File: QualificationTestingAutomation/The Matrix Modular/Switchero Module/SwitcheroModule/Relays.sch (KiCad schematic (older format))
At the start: 5 parts, among them Q1 2N7002DW, U10 TLP3546, U11 TLP3546

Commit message: Cleaned up the libraries Cleaned up the tracks Adjusted footprints to the manufacturers minimum size.
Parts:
- Q1: symbol TheMatrix-rescue:2N7002DW-dk_Transistors-FETs-MOSFETs-Arrays-SchematicAutomation-rescue -> SwitcheroModule-rescue:2N7002DW-dk_Transistors-FETs-MOSFETs-Arrays-SchematicAutomation-rescue-TheMatrix-rescue
- R5, R6: symbol TheMatrix-rescue:RESISTOR-passive-SchematicAutomation-rescue -> SwitcheroModule-rescue:RESISTOR-passive-SchematicAutomation-rescue-TheMatrix-rescue
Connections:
- wire segments 23 -> 25
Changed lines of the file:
@@
 1_Vin
 $Comp
-L TheMatrix-rescue:RESISTOR-passive-SchematicAutomation-rescue R?
+L SwitcheroModule-rescue:RESISTOR-passive-SchematicAutomation-rescue-TheMatrix-rescue R?
 U 1 1 5CB300C6
 P 9650 4900
@@
 	9850 5200 9450 5200
 $Comp
-L TheMatrix-rescue:RESISTOR-passive-SchematicAutomation-rescue R?
+L SwitcheroModule-rescue:RESISTOR-passive-SchematicAutomation-rescue-TheMatrix-rescue R?
 U 1 1 5CB300E1
 P 8500 5500
@@
 	8250 5500 8250 5600
 $Comp
-L power:GND #PWR?
-U 1 1 5CB300F1
-P 9450 5500
-AR Path="/5C90F514/5CB300F1" Ref="#PWR?"  Part="1"
-AR Path="/5C8DF48C/5CB300F1" Ref="#PWR0115"  Part="1"
-F 0 "#PWR0115" H 9450 5250 50  0001 C CNN
-F 1 "GND" H 9455 5327 50  0000 C CNN
-F 2 "" H 9450 5500 50  0001 C CNN
-F 3 "" H 9450 5500 50  0001 C CNN
-	1    9450 5500
-	-1   0    0    1
-$EndComp
-$Comp
 L power:GND #PWR0116
 U 1 1 5CB33E67
@@
 Wire Wire Line
 	9350 3200 9300 3200
-$Comp
-L power:GND #PWR0118
-U 1 1 5CB3980B
-P 8500 4800
-F 0 "#PWR0118" H 8500 4550 50  0001 C CNN
-F 1 "GND" H 8505 4627 50  0000 C CNN
-F 2 "" H 8500 4800 50  0001 C CNN
-F 3 "" H 8500 4800 50  0001 C CNN
-	1    8500 4800
-	-1   0    0    1
-$EndComp
 Wire Wire Line
 	8500 4900 8500 4800
@@
 	8500 4900 8850 4900
 $Comp
-L TheMatrix-rescue:2N7002DW-dk_Transistors-FETs-MOSFETs-Arrays-SchematicAutomation-rescue Q?
+L SwitcheroModule-rescue:2N7002DW-dk_Transistors-FETs-MOSFETs-Arrays-SchematicAutomation-rescue-TheMatrix-rescue Q?
 U 1 1 5CB300A0
 P 9150 5300
@@
 AR Path="/5C90F514/5CB300A0" Ref="Q?"  Part="1"
 AR Path="/5C8DF48C/5CB300A0" Ref="Q1"  Part="1"
+AR Path="/5CB300A0" Ref="Q1"  Part="1"
 F 0 "Q1" H 9150 5787 60  0000 C CNN
 F 1 "2N7002DW" H 9150 5681 60  0000 C CNN
@@
 Wire Wire Line
 	9550 4900 9450 4900
-Wire Wire Line
-	8850 5500 8700 5500
 Text GLabel 8100 5200 0    50   Input ~ 0
 2_REL
@@
 	8100 5200 8850 5200
 Wire Wire Line
-	8700 5500 8700 5600
-Connection ~ 8700 5500
-Wire Wire Line
-	8700 5500 8600 5500
-Text Label 8700 5600 3    50   ~ 0
+	9600 5500 9600 5600
+Text Label 9600 5600 3    50   ~ 0
 1_RELH
 Text Label 8250 3050 1    50   ~ 0
 1_RELH
-Text Label 9550 4750 1    50   ~ 0
+Text Label 8250 4550 1    50   ~ 0
 2_RELH
 Wire Wire Line
@@
 Text Label 9350 3000 1    50   ~ 0
 2_RELH
+Wire Wire Line
+	8600 5500 8850 5500
+Wire Wire Line
+	9600 5500 9450 5500
+Wire Wire Line
+	8500 4800 8250 4800
+Wire Wire Line
+	8250 4800 8250 4550
 $EndSCHEMATC

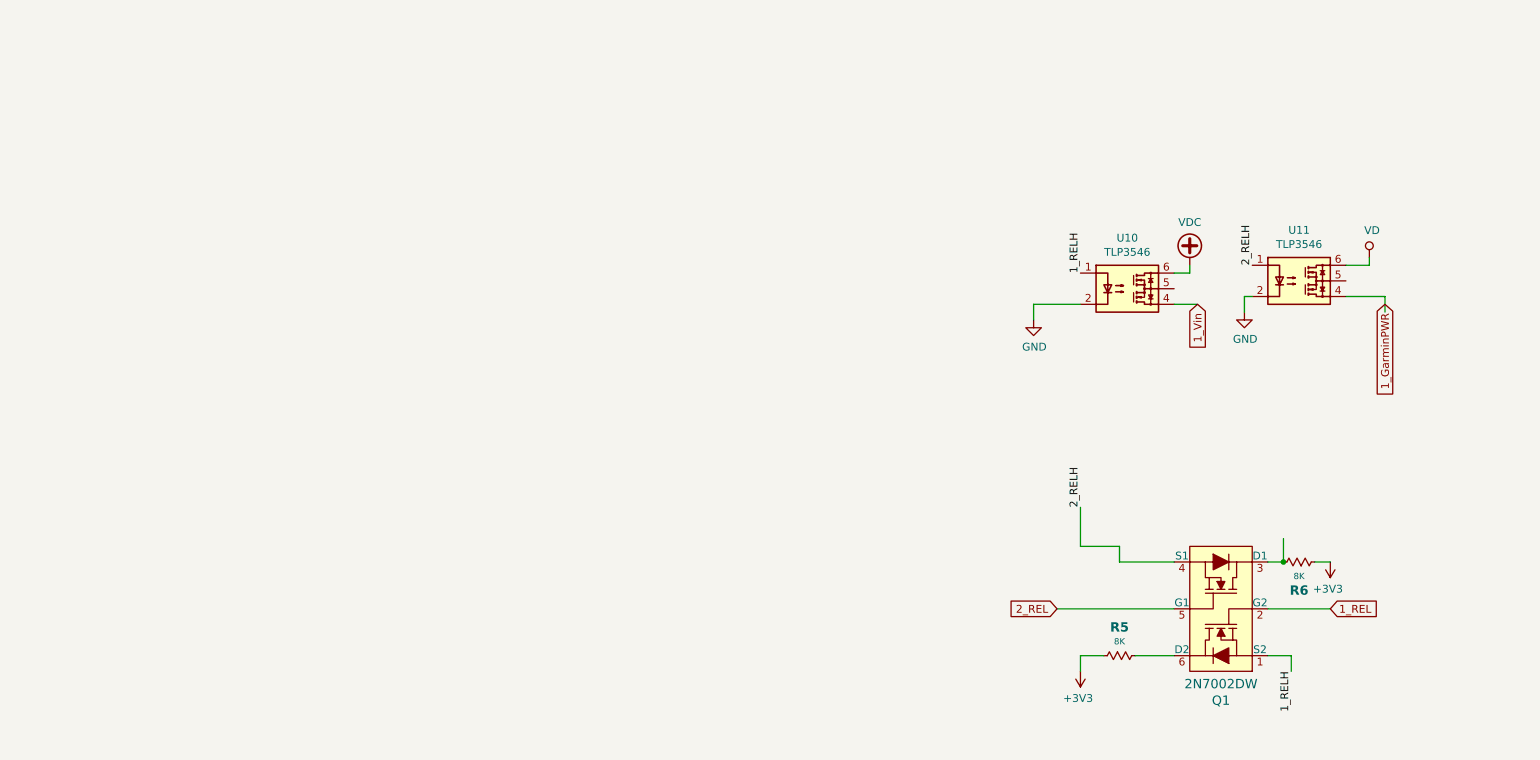
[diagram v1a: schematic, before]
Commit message: Added Voltage and current measurment of the muxes and relays to the MSP Some clean up of the tracks.
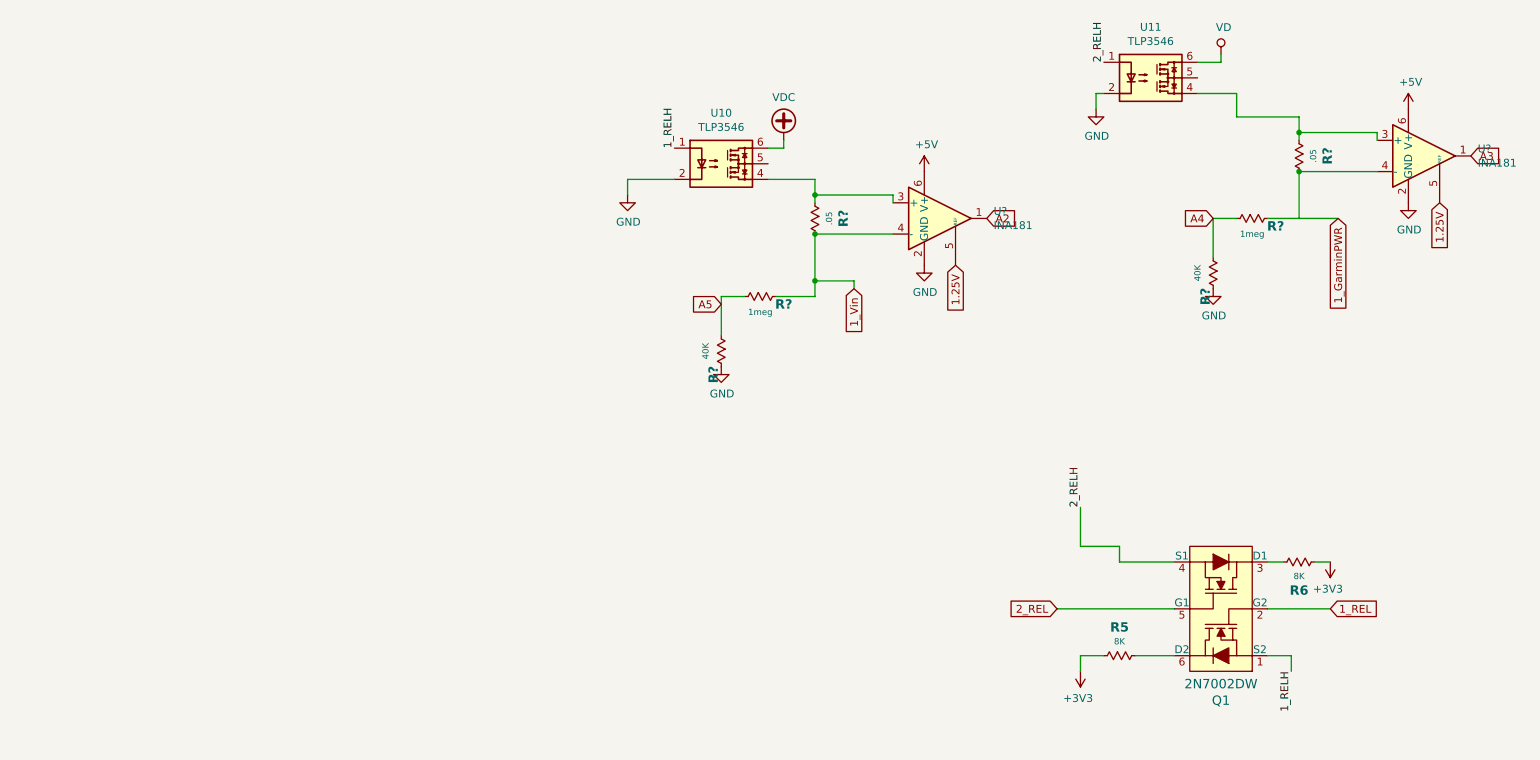
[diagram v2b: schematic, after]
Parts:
- added R? (x2): .05, Resistor_SMD:R_0402_1005Metric, symbol SwitcheroModule-rescue:RESISTOR-passive-SchematicAutomation-rescue-TheMatrix-re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
- added R? (x2): 40K, Resistor_SMD:R_0402_1005Metric, symbol SwitcheroModule-rescue:RESISTOR-passive-SchematicAutomation-rescue-TheMatrix-re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
- added R? (x2): 1meg, Resistor_SMD:R_0402_1005Metric, symbol SwitcheroModule-rescue:RESISTOR-passive-SchematicAutomation-rescue-TheMatrix-re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
- added U? (x2): INA181, Package_TO_SOT_SMD:SOT-23-6, symbol Amplifier_Current:INA181
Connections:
- net labels added: +5V, 1.25V, A2, A3, A4, A5
- wire segments 25 -> 46
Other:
- moved on the sheet: U10, U11

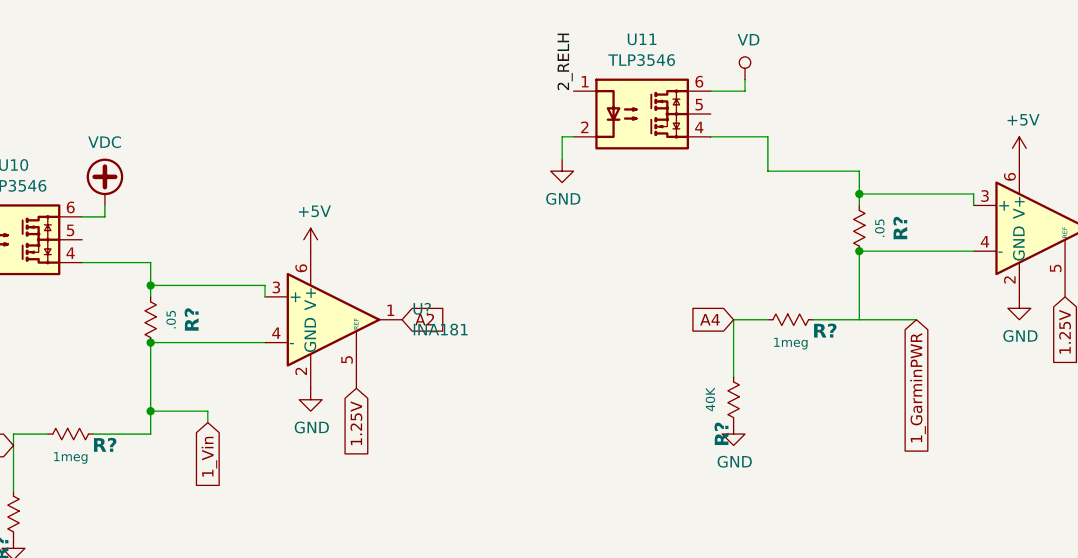
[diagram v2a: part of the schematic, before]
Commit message: Updated the layout to accomodate the voltage and current sensing.
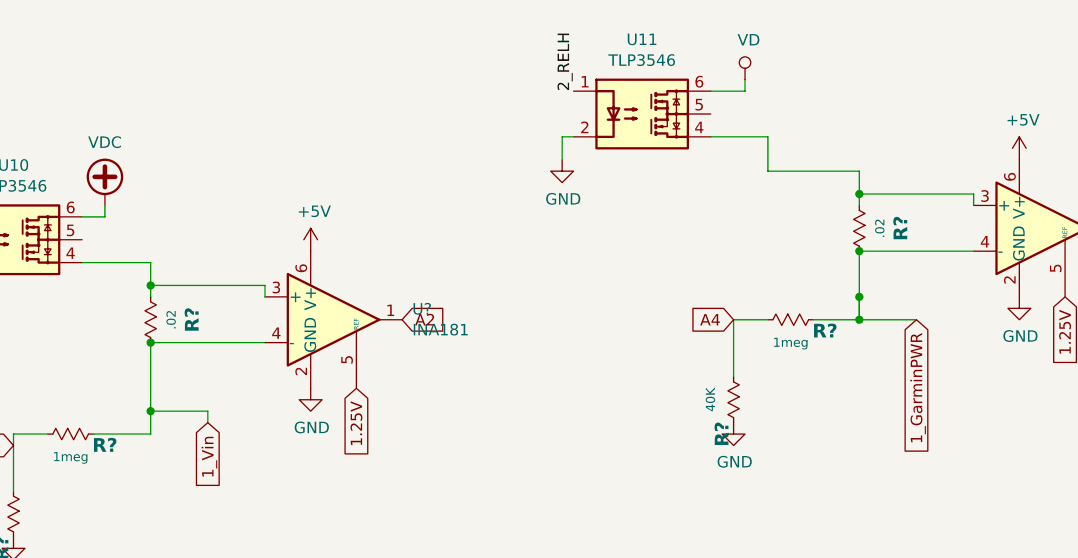
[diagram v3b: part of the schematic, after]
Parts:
- removed R?: .05, Resistor_SMD:R_0402_1005Metric, symbol SwitcheroModule-rescue:RESISTOR-passive-SchematicAutomation-rescue-TheMatrix-re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
- added R?: .02, Resistor_SMD:R_1206_3216Metric_Pad1.42x1.75mm_HandSolder, symbol SwitcheroModule-rescue:RESISTOR-passive-SchematicAutomation-rescue-TheMatrix-re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
- R?: value .05 -> .02; footprint Resistor_SMD:R_0402_1005Metric -> Resistor_SMD:R_1206_3216Metric_Pad1.42x1.75mm_HandSolder; Part - -> PF1206FRF070R02L
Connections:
- net 1_GarminPWR: now also U?.4 (-), R?.2
- net at U11.4, U?.3 (+): now also R?.1
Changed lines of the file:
@@
 AR Path="/5C8DF48C/5C9FB38A" Ref="R?"  Part="1"
 F 0 "R?" H 6550 2882 60  0000 C CNB
-F 1 ".05" H 6550 2791 40  0000 C CNN
-F 2 "Resistor_SMD:R_0402_1005Metric" H 6550 2560 40  0001 C CNN
+F 1 ".02" H 6550 2791 40  0000 C CNN
+F 2 "Resistor_SMD:R_1206_3216Metric_Pad1.42x1.75mm_HandSolder" H 6550 2560 40  0001 C CNN
 F 3 "" H 6550 2800 60  0000 C CNN
-F 4 "-" H 6550 2860 45  0001 C CNN "Part"
+F 4 " PF1206FRF070R02L " H 6550 2860 45  0001 C CNN "Part"
 F 5 "Passive" H 6780 2990 50  0001 C CNN "Family"
 	1    6550 2700
@@
 	1    0    0    -1
 $EndComp
-$Comp
-L SwitcheroModule-rescue:RESISTOR-passive-SchematicAutomation-rescue-TheMatrix-rescue R?
-U 1 1 5CA39606
-P 9650 2300
-AR Path="/5B9C8983/5CA39606" Ref="R?"  Part="1"
-AR Path="/5B9C8983/5C46C371/5CA39606" Ref="R?"  Part="1"
-AR Path="/5B9C8983/5C56517E/5CA39606" Ref="R?"  Part="1"
-AR Path="/5B9C8983/5C583B72/5CA39606" Ref="R?"  Part="1"
-AR Path="/5B9C8983/5C59813F/5CA39606" Ref="R?"  Part="1"
-AR Path="/5B9C8983/5C5B69C1/5CA39606" Ref="R?"  Part="1"
-AR Path="/5B9C8983/5C5D00DA/5CA39606" Ref="R?"  Part="1"
-AR Path="/5BB9E3C7/5BB9E832/5CA39606" Ref="R?"  Part="1"
-AR Path="/5BB9E3C7/5BB9E83C/5CA39606" Ref="R?"  Part="1"
-AR Path="/5BB9E3C7/5BB9E846/5CA39606" Ref="R?"  Part="1"
-AR Path="/5BB9E3C7/5BB9E850/5CA39606" Ref="R?"  Part="1"
-AR Path="/5BB9E3C7/5BB9E85A/5CA39606" Ref="R?"  Part="1"
-AR Path="/5BB9E3C7/5BBCF777/5CA39606" Ref="R?"  Part="1"
-AR Path="/5BB9E3C7/5BBDE28D/5CA39606" Ref="R?"  Part="1"
-AR Path="/5BB9E3C7/5BC04BAF/5CA39606" Ref="R?"  Part="1"
-AR Path="/5BB9E3C7/5BC0E5A0/5CA39606" Ref="R?"  Part="1"
-AR Path="/5BB9E3C7/5BC17F91/5CA39606" Ref="R?"  Part="1"
-AR Path="/5BB9E3C7/5BC2196C/5CA39606" Ref="R?"  Part="1"
-AR Path="/5BB9E3C7/5BD54793/5CA39606" Ref="R?"  Part="1"
-AR Path="/5BB9E3C7/5BD548A9/5CA39606" Ref="R?"  Part="1"
-AR Path="/5BB9E3C7/5BDC515F/5CA39606" Ref="R?"  Part="1"
-AR Path="/5BB9E3C7/5BDC5169/5CA39606" Ref="R?"  Part="1"
-AR Path="/5C90F514/5BB9E85A/5CA39606" Ref="R?"  Part="1"
-AR Path="/5C90F514/5BBDE28D/5CA39606" Ref="R?"  Part="1"
-AR Path="/5C90F514/5C94BFB1/5CA39606" Ref="R?"  Part="1"
-AR Path="/5C90F514/5C94ECF2/5CA39606" Ref="R?"  Part="1"
-AR Path="/5C90F514/5CA39606" Ref="R?"  Part="1"
-AR Path="/5C8DF48C/5CA39606" Ref="R?"  Part="1"
-F 0 "R?" H 9650 2482 60  0000 C CNB
-F 1 ".05" H 9650 2391 40  0000 C CNN
-F 2 "Resistor_SMD:R_0402_1005Metric" H 9650 2160 40  0001 C CNN
-F 3 "" H 9650 2400 60  0000 C CNN
-F 4 "-" H 9650 2460 45  0001 C CNN "Part"
-F 5 "Passive" H 9880 2590 50  0001 C CNN "Family"
-	1    9650 2300
-	0    1    1    0
-$EndComp
 Wire Wire Line
 	9650 2200 9650 2150
@@
 Wire Wire Line
 	10150 2400 9650 2400
-Connection ~ 9650 2400
 $Comp
 L power:GND #PWR?
@@
 $EndComp
 Wire Wire Line
-	9650 2400 9650 2700
+	9650 2400 9650 2600
 Text GLabel 10550 2600 3    50   Input ~ 0
 1.25V
@@
 AR Path="/5C8DF46C/5CA490DA" Ref="R?"  Part="1"
 AR Path="/5C8DF47A/5CA490DA" Ref="R?"  Part="1"
+AR Path="/5C8DF48C/5CA490DA" Ref="R?"  Part="1"
 F 0 "R?" H 6100 3500 60  0000 C CNB
 F 1 "40K" H 5950 3450 40  0000 C CNN
@@
 AR Path="/5C8DF46C/5CA490E2" Ref="R?"  Part="1"
 AR Path="/5C8DF47A/5CA490E2" Ref="R?"  Part="1"
+AR Path="/5C8DF48C/5CA490E2" Ref="R?"  Part="1"
 F 0 "R?" H 6350 3150 60  0000 C CNB
 F 1 "1meg" H 6200 3100 40  0000 C CNN
@@
 U 1 1 5CA490ED
 P 5950 3650
+AR Path="/5C8DF47A/5CA490ED" Ref="#PWR?"  Part="1"
+AR Path="/5C8DF48C/5CA490ED" Ref="#PWR?"  Part="1"
 F 0 "#PWR?" H 5950 3400 50  0001 C CNN
 F 1 "GND" H 5955 3477 50  0000 C CNN
@@
 AR Path="/5C8DF46C/5CA50492" Ref="R?"  Part="1"
 AR Path="/5C8DF47A/5CA50492" Ref="R?"  Part="1"
+AR Path="/5C8DF48C/5CA50492" Ref="R?"  Part="1"
 F 0 "R?" H 9250 3000 60  0000 C CNB
 F 1 "40K" H 9100 2950 40  0000 C CNN
@@
 AR Path="/5C8DF46C/5CA5049A" Ref="R?"  Part="1"
 AR Path="/5C8DF47A/5CA5049A" Ref="R?"  Part="1"
+AR Path="/5C8DF48C/5CA5049A" Ref="R?"  Part="1"
 F 0 "R?" H 9500 2650 60  0000 C CNB
 F 1 "1meg" H 9350 2600 40  0000 C CNN
@@
 U 1 1 5CA504A0
 P 9100 3150
+AR Path="/5C8DF47A/5CA504A0" Ref="#PWR?"  Part="1"
+AR Path="/5C8DF48C/5CA504A0" Ref="#PWR?"  Part="1"
 F 0 "#PWR?" H 9100 2900 50  0001 C CNN
 F 1 "GND" H 9105 2977 50  0000 C CNN
@@
 	9100 2700 9100 2950
 Wire Wire Line
-	9450 2700 9900 2700
+	9450 2700 9650 2700
+$Comp
+L SwitcheroModule-rescue:RESISTOR-passive-SchematicAutomation-rescue-TheMatrix-rescue R?
+U 1 1 5CA79B2A
+P 9650 2300
+AR Path="/5B9C8983/5CA79B2A" Ref="R?"  Part="1"
+AR Path="/5B9C8983/5C46C371/5CA79B2A" Ref="R?"  Part="1"
+AR Path="/5B9C8983/5C56517E/5CA79B2A" Ref="R?"  Part="1"
+AR Path="/5B9C8983/5C583B72/5CA79B2A" Ref="R?"  Part="1"
+AR Path="/5B9C8983/5C59813F/5CA79B2A" Ref="R?"  Part="1"
+AR Path="/5B9C8983/5C5B69C1/5CA79B2A" Ref="R?"  Part="1"
+AR Path="/5B9C8983/5C5D00DA/5CA79B2A" Ref="R?"  Part="1"
+AR Path="/5BB9E3C7/5BB9E832/5CA79B2A" Ref="R?"  Part="1"
+AR Path="/5BB9E3C7/5BB9E83C/5CA79B2A" Ref="R?"  Part="1"
+AR Path="/5BB9E3C7/5BB9E846/5CA79B2A" Ref="R?"  Part="1"
+AR Path="/5BB9E3C7/5BB9E850/5CA79B2A" Ref="R?"  Part="1"
+AR Path="/5BB9E3C7/5BB9E85A/5CA79B2A" Ref="R?"  Part="1"
+AR Path="/5BB9E3C7/5BBCF777/5CA79B2A" Ref="R?"  Part="1"
+AR Path="/5BB9E3C7/5BBDE28D/5CA79B2A" Ref="R?"  Part="1"
+AR Path="/5BB9E3C7/5BC04BAF/5CA79B2A" Ref="R?"  Part="1"
+AR Path="/5BB9E3C7/5BC0E5A0/5CA79B2A" Ref="R?"  Part="1"
+AR Path="/5BB9E3C7/5BC17F91/5CA79B2A" Ref="R?"  Part="1"
+AR Path="/5BB9E3C7/5BC2196C/5CA79B2A" Ref="R?"  Part="1"
+AR Path="/5BB9E3C7/5BD54793/5CA79B2A" Ref="R?"  Part="1"
+AR Path="/5BB9E3C7/5BD548A9/5CA79B2A" Ref="R?"  Part="1"
+AR Path="/5BB9E3C7/5BDC515F/5CA79B2A" Ref="R?"  Part="1"
+AR Path="/5BB9E3C7/5BDC5169/5CA79B2A" Ref="R?"  Part="1"
+AR Path="/5C90F514/5BB9E85A/5CA79B2A" Ref="R?"  Part="1"
+AR Path="/5C90F514/5BBDE28D/5CA79B2A" Ref="R?"  Part="1"
+AR Path="/5C90F514/5C94BFB1/5CA79B2A" Ref="R?"  Part="1"
+AR Path="/5C90F514/5C94ECF2/5CA79B2A" Ref="R?"  Part="1"
+AR Path="/5C90F514/5CA79B2A" Ref="R?"  Part="1"
+AR Path="/5C8DF48C/5CA79B2A" Ref="R?"  Part="1"
+F 0 "R?" H 9650 2482 60  0000 C CNB
+F 1 ".02" H 9650 2391 40  0000 C CNN
+F 2 "Resistor_SMD:R_1206_3216Metric_Pad1.42x1.75mm_HandSolder" H 9650 2160 40  0001 C CNN
+F 3 "" H 9650 2400 60  0000 C CNN
+F 4 " PF1206FRF070R02L " H 9650 2460 45  0001 C CNN "Part"
+F 5 "Passive" H 9880 2590 50  0001 C CNN "Family"
+	1    9650 2300
+	0    1    1    0
+$EndComp
+Connection ~ 9650 2400
+Wire Wire Line
+	9650 2700 9650 2600
+Connection ~ 9650 2700
+Wire Wire Line
+	9650 2700 9900 2700
+Connection ~ 9650 2600
+Wire Wire Line
+	9650 2600 9650 2700
 $EndSCHEMATC
